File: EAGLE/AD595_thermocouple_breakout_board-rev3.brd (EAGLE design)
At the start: 30.9 x 42.5 mm, 7 parts

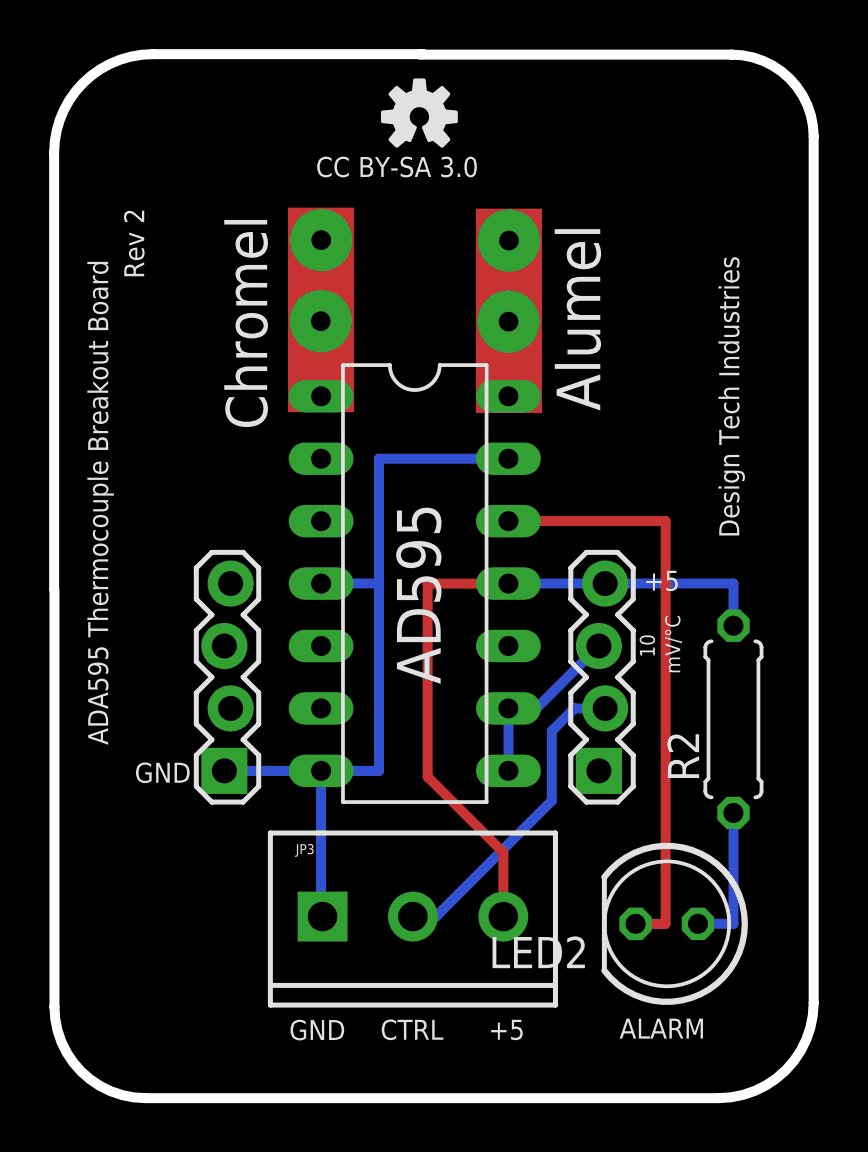
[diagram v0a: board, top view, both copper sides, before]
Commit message: Commit of revision three of board. Now includes a program status LED. This version is more part of a toaster reflow oven controller than anything else (hence keeping revision two active).
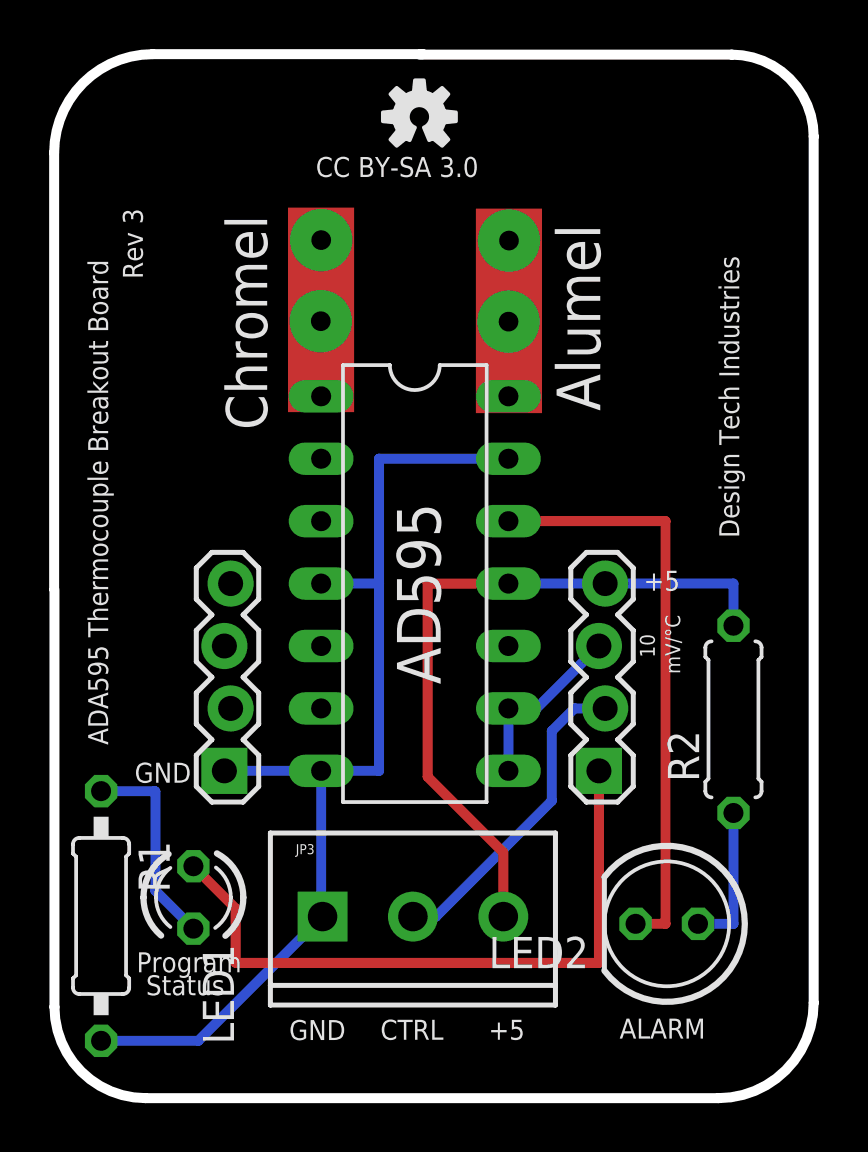
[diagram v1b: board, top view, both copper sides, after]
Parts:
- added LED1: (no value), led:LED3MM
- added R1: 220, resistor:0207/10
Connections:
- new net N$4: LED1.K, R1.1
- new net N$5: JP2.1, LED1.A
- net GND: now also R1.2
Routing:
- net N$5: track 0.00 -> 27.2 mm
- net GND: track 32.6 -> 43.7 mm
- net N$4: track 0.00 -> 8.43 mm
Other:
- board text added: "Program"
- board text added: "Rev 3"
- board text added: "Status"
- board text removed: "Rev 2"
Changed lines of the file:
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@@
 <wire x1="38.869996875" y1="64.722653125" x2="34.856115625" y2="60.708771875" width="0.4064" layer="20" curve="90"/>
 <wire x1="34.856115625" y1="60.708771875" x2="34.856115625" y2="42.960340625" width="0.4064" layer="20"/>
-<text x="38.521540625" y="55.587390625" size="0.8128" layer="21" rot="R90">Rev 2</text>
 <text x="57.86089375" y="24.665534375" size="0.8128" layer="21">ALARM</text>
+<text x="38.211353125" y="27.363621875" size="0.8128" layer="21">Program</text>
+<text x="38.593471875" y="26.428803125" size="0.8128" layer="21">Status</text>
+<text x="38.46616875" y="55.576928125" size="0.8128" layer="21" rot="R90">Rev 3</text>
 </plain>
 <attributes>
@@
 <element name="R2" library="rcl" package="0207/7" value="330" x="62.497009375" y="37.655396875" rot="R90"/>
 <element name="JP3" library="SparkFun-Connectors" package="SCREWTERMINAL-3.5MM-3_LOCK.007S" value="" x="45.955103125" y="29.6299125"/>
+<element name="R1" library="resistor" package="0207/10" value="220" x="36.76629375" y="29.654703125" rot="R270"/>
+<element name="LED1" library="led" package="LED3MM" value="" x="40.522446875" y="30.408471875" rot="R270"/>
 </elements>
 <signals>
@@
 <wire x1="45.777303125" y1="29.6299125" x2="45.72" y2="29.6299125" width="0.4064" layer="16"/>
 <wire x1="45.72" y1="29.6299125" x2="45.72" y2="35.56" width="0.4064" layer="16"/>
+<contactref element="R1" pad="2"/>
+<wire x1="36.76629375" y1="24.574703125" x2="40.72209375" y2="24.574703125" width="0.4064" layer="16"/>
+<wire x1="40.72209375" y1="24.574703125" x2="45.777303125" y2="29.6299125" width="0.4064" layer="16"/>
 </signal>
 <signal name="VCC">
@@
 <wire x1="53.345996875" y1="53.838653125" x2="53.363571875" y2="57.138315625" width="0" layer="19" extent="1-1"/>
 </signal>
+<signal name="N$4">
+<contactref element="R1" pad="1"/>
+<contactref element="LED1" pad="K"/>
+<wire x1="40.522446875" y1="29.138471875" x2="38.9755875" y2="30.68533125" width="0.4064" layer="16"/>
+<wire x1="38.9755875" y1="30.68533125" x2="38.9755875" y2="34.714384375" width="0.4064" layer="16"/>
+<wire x1="38.9755875" y1="34.714384375" x2="38.95526875" y2="34.734703125" width="0.4064" layer="16"/>
+<wire x1="38.95526875" y1="34.734703125" x2="36.76629375" y2="34.734703125" width="0.4064" layer="16"/>
+</signal>
+<signal name="N$5">
+<contactref element="LED1" pad="A"/>
+<contactref element="JP2" pad="1"/>
+<wire x1="40.522446875" y1="31.678471875" x2="42.244771875" y2="29.956146875" width="0.4064" layer="1"/>
+<wire x1="42.244771875" y1="29.956146875" x2="42.244771875" y2="27.746046875" width="0.4064" layer="1"/>
+<wire x1="42.244771875" y1="27.746046875" x2="57.023" y2="27.746046875" width="0.4064" layer="1"/>
+<wire x1="57.023" y1="27.746046875" x2="57.023" y2="35.56" width="0.4064" layer="1"/>
+</signal>
 </signals>
-<errors>
-</errors>
 </board>
 </drawing>

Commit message: Minor change to status LED and resistor in revision 3.
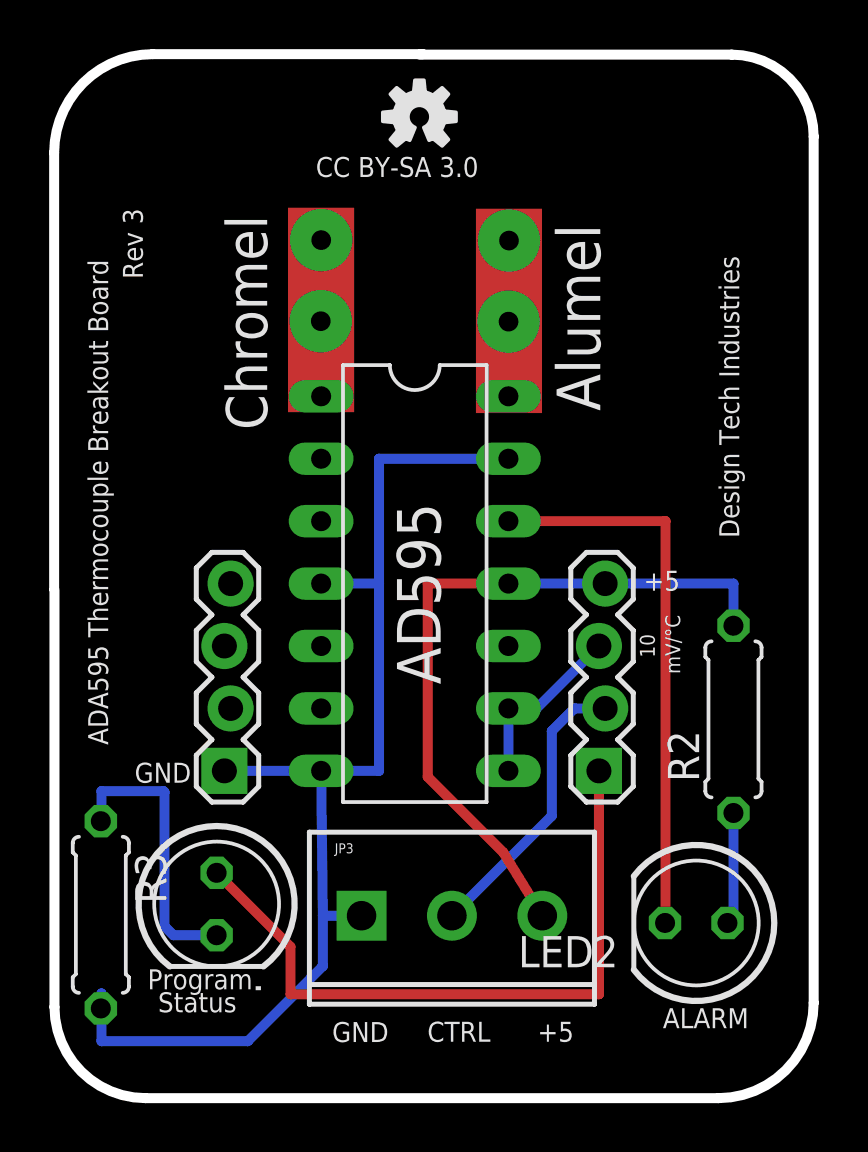
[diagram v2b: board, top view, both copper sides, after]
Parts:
- removed LED1: (no value), led:LED3MM
- removed R1: 220, resistor:0207/10
- added .: (no value), led:LED5MM
- added R3: 330, rcl:0207/7
- moved JP3 1.59 mm to (47.5, 29.7)
- moved LED2 1.20 mm to (61.0, 29.4)
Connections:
- net GND: now also R3.2; no longer R1.2
- net N$4: now also ..K, R3.1; no longer LED1.K, R1.1
- net N$5: now also ..A; no longer LED1.A
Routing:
- net GND: track 43.7 -> 49.0 mm
- net N$4: track 8.43 -> 11.5 mm
- net N$1: track 13.0 -> 11.8 mm
- net N$7: track 5.95 -> 4.76 mm
- net N$8: track 24.0 -> 22.8 mm
- net N$5: track 27.2 -> 27.8 mm
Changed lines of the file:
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@@
 <text x="60.3314" y="39.5024" size="0.6096" layer="21" ratio="9" rot="R90">mV/°C</text>
 <text x="50.5831" y="39.0801" size="1.778" layer="21" rot="R90">AD595</text>
-<text x="52.5316375" y="24.618184375" size="0.8128" layer="21" ratio="9">+5</text>
-<text x="44.41629375" y="24.606659375" size="0.8128" layer="21" ratio="9">GND</text>
-<text x="48.12915625" y="24.618178125" size="0.8128" layer="21">CTRL</text>
+<text x="54.525434375" y="24.536703125" size="0.8128" layer="21" ratio="9">+5</text>
+<text x="46.165946875" y="24.525278125" size="0.8128" layer="21" ratio="9">GND</text>
+<text x="50.041571875" y="24.536796875" size="0.8128" layer="21">CTRL</text>
 <text x="45.5014" y="59.7245" size="0.8128" layer="21">CC BY-SA 3.0</text>
 <text x="62.7328" y="45.0376" size="0.8128" layer="21" rot="R90">Design Tech Industries</text>
@@
 <wire x1="38.869996875" y1="64.722653125" x2="34.856115625" y2="60.708771875" width="0.4064" layer="20" curve="90"/>
 <wire x1="34.856115625" y1="60.708771875" x2="34.856115625" y2="42.960340625" width="0.4064" layer="20"/>
-<text x="57.86089375" y="24.665534375" size="0.8128" layer="21">ALARM</text>
-<text x="38.211353125" y="27.363621875" size="0.8128" layer="21">Program</text>
-<text x="38.593471875" y="26.428803125" size="0.8128" layer="21">Status</text>
+<text x="59.623859375" y="25.0889" size="0.8128" layer="21">ALARM</text>
+<text x="38.658903125" y="26.67131875" size="0.8128" layer="21">Program</text>
+<text x="39.0817625" y="25.736603125" size="0.8128" layer="21">Status</text>
 <text x="38.46616875" y="55.576928125" size="0.8128" layer="21" rot="R90">Rev 3</text>
 </plain>
@@
 </element>
 <element name="U$1" library="SparkFun" package="OSHW-LOGO-S" value="OSHW-LOGOS" x="49.7187" y="62.1718"/>
-<element name="LED2" library="led" package="LED5MM" value="" x="59.784690625" y="29.33496875" rot="R180"/>
+<element name="LED2" library="led" package="LED5MM" value="" x="60.983571875" y="29.370225" rot="R180"/>
 <element name="R2" library="rcl" package="0207/7" value="330" x="62.497009375" y="37.655396875" rot="R90"/>
-<element name="JP3" library="SparkFun-Connectors" package="SCREWTERMINAL-3.5MM-3_LOCK.007S" value="" x="45.955103125" y="29.6299125"/>
-<element name="R1" library="resistor" package="0207/10" value="220" x="36.76629375" y="29.654703125" rot="R270"/>
-<element name="LED1" library="led" package="LED3MM" value="" x="40.522446875" y="30.408471875" rot="R270"/>
+<element name="JP3" library="SparkFun-Connectors" package="SCREWTERMINAL-3.5MM-3_LOCK.007S" value="" x="47.541790625" y="29.665165625"/>
+<element name="." library="led" package="LED5MM" value="" x="41.46723125" y="30.140859375" rot="R270"/>
+<element name="R3" library="rcl" package="0207/7" value="330" x="36.75573125" y="29.702353125" rot="R270"/>
 </elements>
 <signals>
@@
 <wire x1="48.0764" y1="35.56" x2="48.0764" y2="43.18" width="0.4064" layer="16"/>
 <contactref element="JP3" pad="1"/>
-<wire x1="45.777303125" y1="29.6299125" x2="45.72" y2="29.6299125" width="0.4064" layer="16"/>
-<wire x1="45.72" y1="29.6299125" x2="45.72" y2="35.56" width="0.4064" layer="16"/>
-<contactref element="R1" pad="2"/>
-<wire x1="36.76629375" y1="24.574703125" x2="40.72209375" y2="24.574703125" width="0.4064" layer="16"/>
-<wire x1="40.72209375" y1="24.574703125" x2="45.777303125" y2="29.6299125" width="0.4064" layer="16"/>
+<wire x1="47.363990625" y1="29.665165625" x2="45.7905125" y2="29.665165625" width="0.4064" layer="16"/>
+<wire x1="45.7905125" y1="29.665165625" x2="45.72" y2="35.56" width="0.4064" layer="16"/>
+<wire x1="45.7905125" y1="29.665165625" x2="45.7905125" y2="27.61559375" width="0.4064" layer="16"/>
+<wire x1="45.7905125" y1="27.61559375" x2="42.734584375" y2="24.559665625" width="0.4064" layer="16"/>
+<wire x1="42.734584375" y1="24.559665625" x2="36.78133125" y2="24.559665625" width="0.4064" layer="16"/>
+<contactref element="R3" pad="2"/>
+<wire x1="36.75573125" y1="25.892353125" x2="36.78133125" y2="26.503171875" width="0.4064" layer="16"/>
+<wire x1="36.78133125" y1="26.503171875" x2="36.78133125" y2="24.559665625" width="0.4064" layer="16"/>
 </signal>
 <signal name="VCC">
@@
 <wire x1="57.277" y1="43.18" x2="62.497009375" y2="43.18" width="0.4064" layer="16"/>
 <wire x1="62.497009375" y1="43.18" x2="62.497009375" y2="41.465396875" width="0.4064" layer="16"/>
-<wire x1="53.132903125" y1="29.6299125" x2="53.132903125" y2="32.2407625" width="0.4064" layer="1"/>
+<wire x1="54.719590625" y1="29.665165625" x2="53.132903125" y2="32.2407625" width="0.4064" layer="1"/>
 <wire x1="53.132903125" y1="32.2407625" x2="50.054153125" y2="35.3195125" width="0.4064" layer="1"/>
 <wire x1="50.054153125" y1="35.3195125" x2="50.054153125" y2="43.1791875" width="0.4064" layer="1"/>
@@
 <contactref element="JP2" pad="2"/>
 <contactref element="JP3" pad="2"/>
-<wire x1="49.455103125" y1="29.6299125" x2="50.394003125" y2="29.6299125" width="0.4064" layer="16"/>
-<wire x1="50.394003125" y1="29.6299125" x2="55.105196875" y2="34.34110625" width="0.4064" layer="16"/>
-<wire x1="55.105196875" y1="34.34110625" x2="55.105196875" y2="37.178890625" width="0.4064" layer="16"/>
+<wire x1="55.105196875" y1="33.728571875" x2="55.105196875" y2="37.178890625" width="0.4064" layer="16"/>
 <wire x1="55.105196875" y1="37.178890625" x2="56.02630625" y2="38.1" width="0.4064" layer="16"/>
 <wire x1="57.277" y1="38.1" x2="56.02630625" y2="38.1" width="0.4064" layer="16"/>
+<wire x1="55.105196875" y1="33.728571875" x2="51.041790625" y2="29.665165625" width="0.4064" layer="16"/>
 </signal>
 <signal name="N$7">
 <contactref element="R2" pad="1"/>
 <contactref element="LED2" pad="A"/>
-<wire x1="61.054690625" y1="29.33496875" x2="62.497009375" y2="29.33496875" width="0.4064" layer="16"/>
+<wire x1="62.253571875" y1="29.370225" x2="62.497009375" y2="29.33496875" width="0.4064" layer="16"/>
 <wire x1="62.497009375" y1="29.33496875" x2="62.497009375" y2="33.845396875" width="0.4064" layer="16"/>
 </signal>
@@
 <contactref element="LED2" pad="K"/>
 <contactref element="IC1" pad="12"/>
-<wire x1="58.514690625" y1="29.33496875" x2="59.732671875" y2="29.33496875" width="0.4064" layer="1"/>
+<wire x1="59.713571875" y1="29.370225" x2="59.732671875" y2="29.33496875" width="0.4064" layer="1"/>
 <wire x1="59.732671875" y1="29.33496875" x2="59.732671875" y2="45.722946875" width="0.4064" layer="1"/>
 <wire x1="59.732671875" y1="45.722946875" x2="53.34" y2="45.722946875" width="0.4064" layer="1"/>
@@
 </signal>
 <signal name="N$4">
-<contactref element="R1" pad="1"/>
-<contactref element="LED1" pad="K"/>
-<wire x1="40.522446875" y1="29.138471875" x2="38.9755875" y2="30.68533125" width="0.4064" layer="16"/>
-<wire x1="38.9755875" y1="30.68533125" x2="38.9755875" y2="34.714384375" width="0.4064" layer="16"/>
-<wire x1="38.9755875" y1="34.714384375" x2="38.95526875" y2="34.734703125" width="0.4064" layer="16"/>
-<wire x1="38.95526875" y1="34.734703125" x2="36.76629375" y2="34.734703125" width="0.4064" layer="16"/>
+<contactref element="." pad="K"/>
+<wire x1="41.46723125" y1="28.870859375" x2="39.712796875" y2="28.870859375" width="0.4064" layer="16"/>
+<wire x1="39.712796875" y1="28.870859375" x2="39.346225" y2="29.23743125" width="0.4064" layer="16"/>
+<wire x1="39.346225" y1="29.23743125" x2="39.346225" y2="34.6940625" width="0.4064" layer="16"/>
+<wire x1="39.346225" y1="34.6940625" x2="39.305584375" y2="34.734703125" width="0.4064" layer="16"/>
+<contactref element="R3" pad="1"/>
+<wire x1="36.75573125" y1="33.512353125" x2="36.78285625" y2="34.123171875" width="0.4064" layer="16"/>
+<wire x1="36.78285625" y1="34.123171875" x2="36.78285625" y2="34.734703125" width="0.4064" layer="16"/>
+<wire x1="36.78285625" y1="34.734703125" x2="39.305584375" y2="34.734703125" width="0.4064" layer="16"/>
 </signal>
 <signal name="N$5">
-<contactref element="LED1" pad="A"/>
 <contactref element="JP2" pad="1"/>
-<wire x1="40.522446875" y1="31.678471875" x2="42.244771875" y2="29.956146875" width="0.4064" layer="1"/>
-<wire x1="42.244771875" y1="29.956146875" x2="42.244771875" y2="27.746046875" width="0.4064" layer="1"/>
-<wire x1="42.244771875" y1="27.746046875" x2="57.023" y2="27.746046875" width="0.4064" layer="1"/>
-<wire x1="57.023" y1="27.746046875" x2="57.023" y2="35.56" width="0.4064" layer="1"/>
+<contactref element="." pad="A"/>
+<wire x1="41.46723125" y1="31.410859375" x2="44.4730625" y2="28.405028125" width="0.4064" layer="1"/>
+<wire x1="44.4730625" y1="28.405028125" x2="44.4730625" y2="26.468425" width="0.4064" layer="1"/>
+<wire x1="44.4730625" y1="26.468425" x2="57.023" y2="26.468425" width="0.4064" layer="1"/>
+<wire x1="57.023" y1="26.468425" x2="57.023" y2="35.56" width="0.4064" layer="1"/>
 </signal>
 </signals>
